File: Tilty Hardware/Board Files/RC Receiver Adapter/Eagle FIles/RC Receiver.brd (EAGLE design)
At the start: 38.1 x 50.8 mm, 19 parts, among them U1 ATMEGA328P, U2 LM2931, Y1 16MHz

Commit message: Finally got TiltyIMU class working! updated some other programs, worked on RC receiver add-on
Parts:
- removed JP5: 18_PIN_HEADER3X6_PTH_HEADER, My Parts:3X6_PTH_HEADER
- added JP7: 18_PIN_HEADER3X6_PTH_HEADER, My Parts:3X6_PTH_HEADER
- added U$1: C74HC407514-SOIC, My Parts:14-SOIC
- Y1: device SparkFun-FreqCtrl:HC49UP -> SparkFun-FreqCtrl:CRYSTAL-SMD-5X3
- moved R3 91.3 mm to (-52.1, 52.1), turned to 0 degrees
- moved R2 86.1 mm to (-48.3, 52.1), turned to 0 degrees
- moved JP6 61.3 mm to (-36.8, 34.3), turned to 0 degrees
- moved R1 59.7 mm to (-41.9, 43.2), turned to 0 degrees
- moved S1 49.5 mm to (-35.6, 43.2), turned to 0 degrees
- moved C2 31.7 mm to (10.0, 37.1), turned to 270 degrees
- moved C6 26.4 mm to (2.54, 7.62)
- moved U2 25.7 mm to (7.62, 6.86), turned to 180 degrees
- moved Y1 21.8 mm to (11.2, 32.5), turned to 90 degrees
- moved C1 19.3 mm to (14.0, 31.2)
- moved C7 18.2 mm to (11.9, 10.4)
- moved C3 7.52 mm to (18.3, 19.3), turned to 0 degrees
- moved U1 5.08 mm to (19.1, 25.4), turned to 270 degrees
- moved SJ1 0.40 mm to (5.97, 13.8)
- turned JP4 to 90 degrees
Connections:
- new net EVEN_CHAN: U$1.P$12, U1.1
- new net ODD_CHAN: U$1.P$4, U1.32
- net +5V: now also JP7.11, JP7.14, JP7.17, JP7.2, JP7.5, JP7.8, U$1.P$14; no longer JP5.11, JP5.14, JP5.17, JP5.2, JP5.5, JP5.8
- net GND: now also JP7.12, JP7.15, JP7.18, JP7.3, JP7.6, JP7.9, U$1.P$13; no longer JP5.12, JP5.15, JP5.18, JP5.3, JP5.6, JP5.9
- net N$1: now also Y1.3; no longer Y1.2
- net SIGNAL_1: now also JP7.1, U$1.P$1; no longer JP5.1, U1.32
- net SIGNAL_2: now also JP7.4, U$1.P$11; no longer JP5.4, U1.1
- net SIGNAL_3: now also JP7.7, U$1.P$2; no longer JP5.7, U1.2
- net SIGNAL_4: now also JP7.10, U$1.P$10; no longer JP5.10, U1.9
- net SIGNAL_5: now also JP7.13, U$1.P$3; no longer JP5.13, U1.10
- net SIGNAL_6: now also JP7.16, U$1.P$9; no longer JP5.16, U1.11
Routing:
- net GND: track 12.7 -> 0.00 mm
- net +5V: track 12.7 -> 0.00 mm

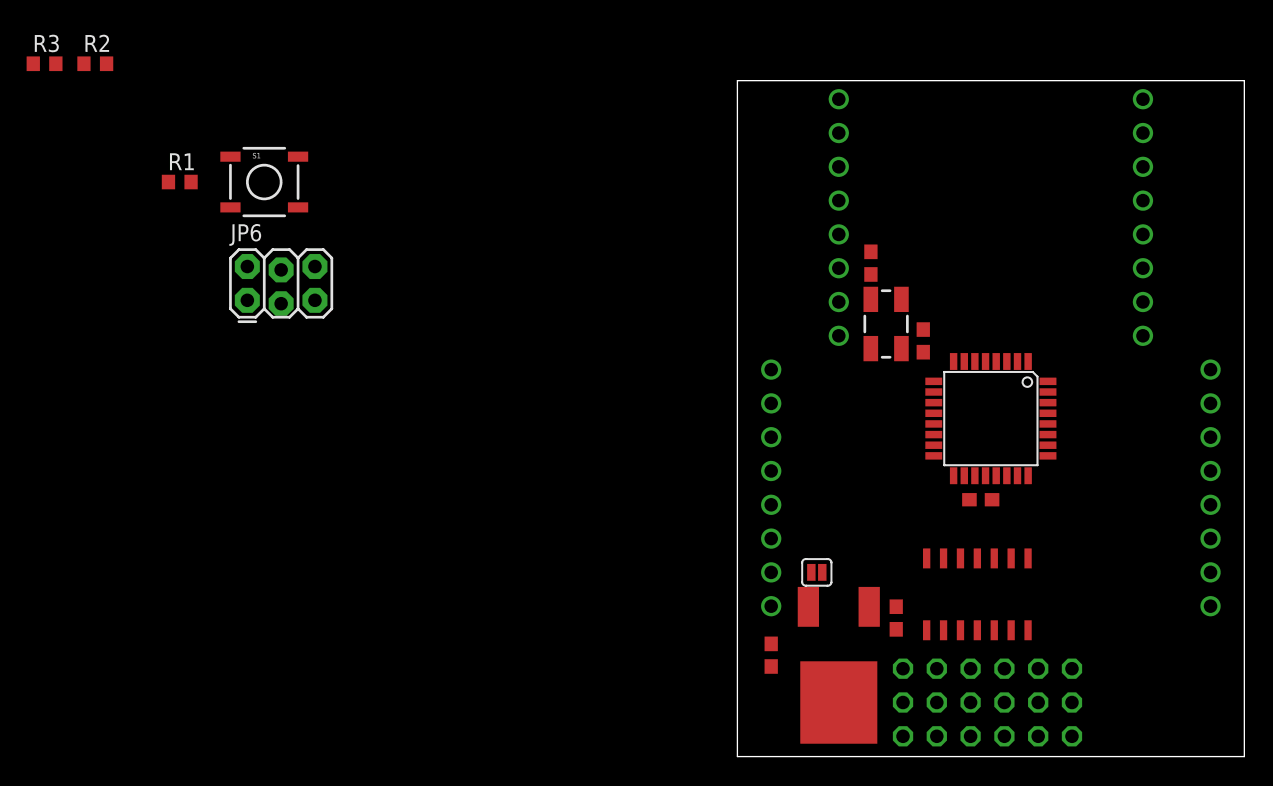
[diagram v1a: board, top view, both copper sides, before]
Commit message: Nearly finished R/C receiver add-on, updated things to-do
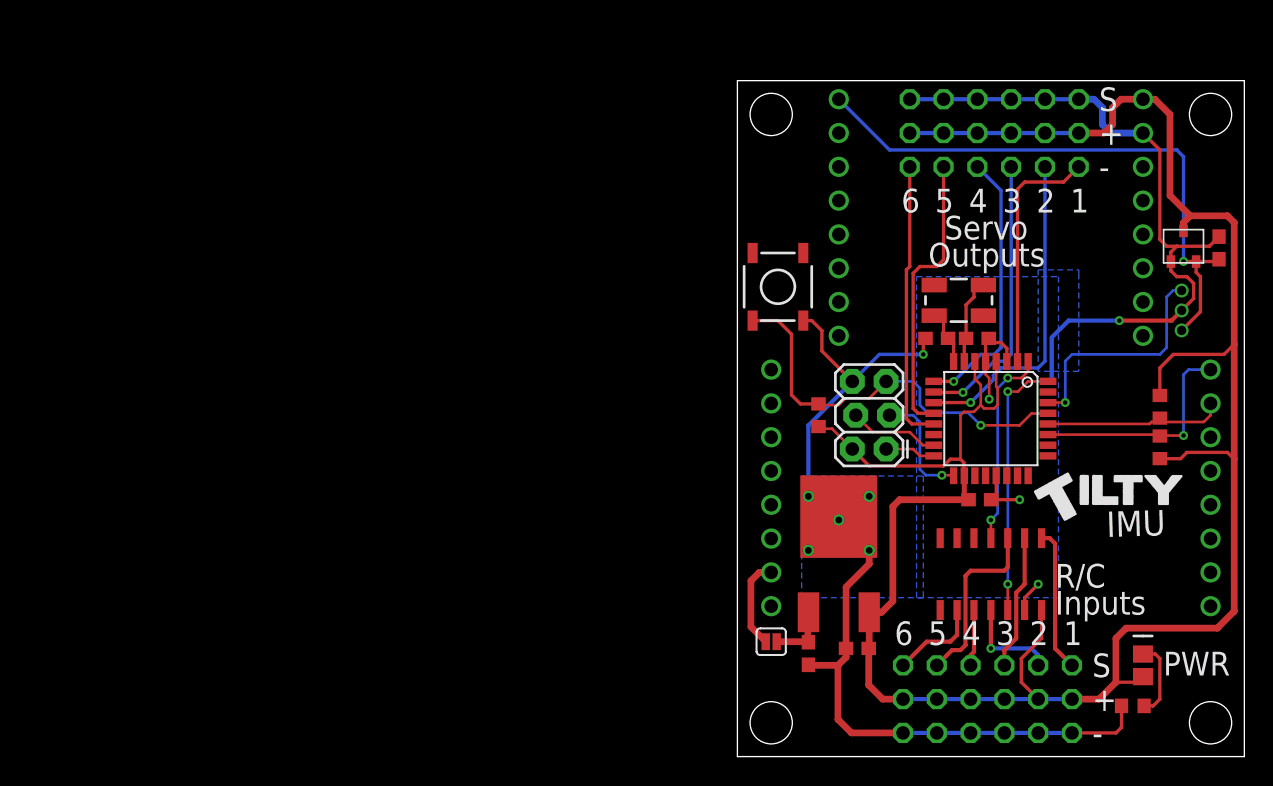
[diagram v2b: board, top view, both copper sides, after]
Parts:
- removed U$1: C74HC407514-SOIC, My Parts:14-SOIC
- added C4: 0.1uF, resistor:C0603
- added D1: (no value), SparkFun-LED:LED-0805
- added JP5: Output, My Parts:3X6_PTH_HEADER
- added JP8: 3-PIN_JST_ZH_PTH_CONNECTORRIGHT_ANGLE_PTH, My Parts:3-PIN_JST_ZH_CONNECTOR_TH
- added R4: 220, resistor:R0603
- added U3: AP7313SOT23R, My Parts:SOT23
- added U4: C74HC407514-SOIC, My Parts:14-SOIC
- JP7: value 18_PIN_HEADER3X6_PTH_HEADER -> Input
- moved R3 87.7 mm to (31.8, 26.3), turned to 90 degrees
- moved R2 85.0 mm to (31.8, 23.2), turned to 270 degrees
- moved R1 51.1 mm to (6.10, 25.7), turned to 90 degrees
- moved JP6 49.3 mm to (11.2, 23.1), turned to 90 degrees
- moved S1 39.4 mm to (3.05, 35.3), turned to 90 degrees
- moved C2 9.80 mm to (18.0, 31.4), turned to 180 degrees
- moved U2 8.38 mm to (7.62, 15.2), turned to 0 degrees
- moved C7 7.12 mm to (5.33, 7.75)
- moved C6 6.50 mm to (9.02, 8.13), turned to 180 degrees
- moved SJ1 6.23 mm to (2.54, 8.64)
- moved Y1 5.74 mm to (16.6, 34.3), turned to 0 degrees
- moved C1 1.03 mm to (15.0, 31.4), turned to 0 degrees
- moved JP7 0.25 mm to (18.8, 4.32)
- moved C3 0.06 mm to (18.2, 19.3)
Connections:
- new net +3V3: C4.1, JP1.8, JP8.P$1, U3.P$2
- new net N$8: D1.2, R4.2
- new net SATELLITE_TX: JP8.P$3, U1.30
- new net SERVO_1: JP5.1, U1.13
- new net SERVO_2: JP5.4, U1.12
- new net SERVO_3: JP5.7, U1.9
- new net SERVO_4: JP5.10, U1.10
- new net SERVO_5: JP5.13, U1.11
- new net SERVO_6: JP5.16, U1.2
- net +5V: now also D1.1, JP4.8, JP5.11, JP5.14, JP5.17, JP5.2, JP5.5, JP5.8, U3.P$3, U4.P$14; no longer U$1.P$14
- net EVEN_CHAN: now also U1.32, U4.P$12; no longer U$1.P$12, U1.1
- net GND: now also C4.2, JP4.7, JP5.12, JP5.15, JP5.18, JP5.3, JP5.6, JP5.9, JP8.P$2, R4.1, U3.P$1, U4.P$13; no longer U$1.P$13
- net ODD_CHAN: now also U1.1, U4.P$4; no longer U$1.P$4, U1.32
- net SIGNAL_1: now also U4.P$1; no longer U$1.P$1
- net SIGNAL_2: now also U4.P$11; no longer U$1.P$11
- net SIGNAL_3: now also U4.P$2; no longer U$1.P$2
- net SIGNAL_4: now also U4.P$10; no longer U$1.P$10
- net SIGNAL_5: now also U4.P$3; no longer U$1.P$3
- net SIGNAL_6: now also U4.P$9; no longer U$1.P$9
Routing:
- net +5V: track 0.00 -> 170.6 mm
- net GND: track 0.00 -> 130.5 mm, vias 0 -> 10
- net +3V3: track 0.00 -> 44.2 mm, vias 0 -> 1
- net RESET: track 0.00 -> 30.8 mm, vias 0 -> 1
- net SERVO_5: track 0.00 -> 24.4 mm, vias 0 -> 1
- net SERVO_2: track 0.00 -> 21.6 mm
- net SERVO_1: track 0.00 -> 21.3 mm
- net SERVO_4: track 0.00 -> 21.1 mm, vias 0 -> 1
- net SERVO_3: track 0.00 -> 20.4 mm, vias 0 -> 1
- net EVEN_CHAN: track 0.00 -> 19.8 mm, vias 0 -> 2
- net SERVO_6: track 0.00 -> 18.2 mm
- net SATELLITE_TX: track 0.00 -> 17.6 mm, vias 0 -> 1
- net SDA: track 0.00 -> 17.0 mm, vias 0 -> 1
- net ODD_CHAN: track 0.00 -> 15.0 mm, vias 0 -> 2
- net SIGNAL_5: track 0.00 -> 13.6 mm
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- added copper zone on layer 16, net GND
- added copper zone on layer 16, net N$3
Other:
- board text added: "+"
- board text added: "-"
- board text added: "1"
- board text added: "2"
- board text added: "3"
- board text added: "4"
- board text added: "5"
- board text added: "6"
- board text added: "Add-on"
- board text added: "IMU"
- board text added: "Inputs"
- board text added: "Outputs"
- board text added: "PWR"
- board text added: "R/C"
- board text added: "R/C Receiver"
- board text added: "S"
- board text added: "Servo"

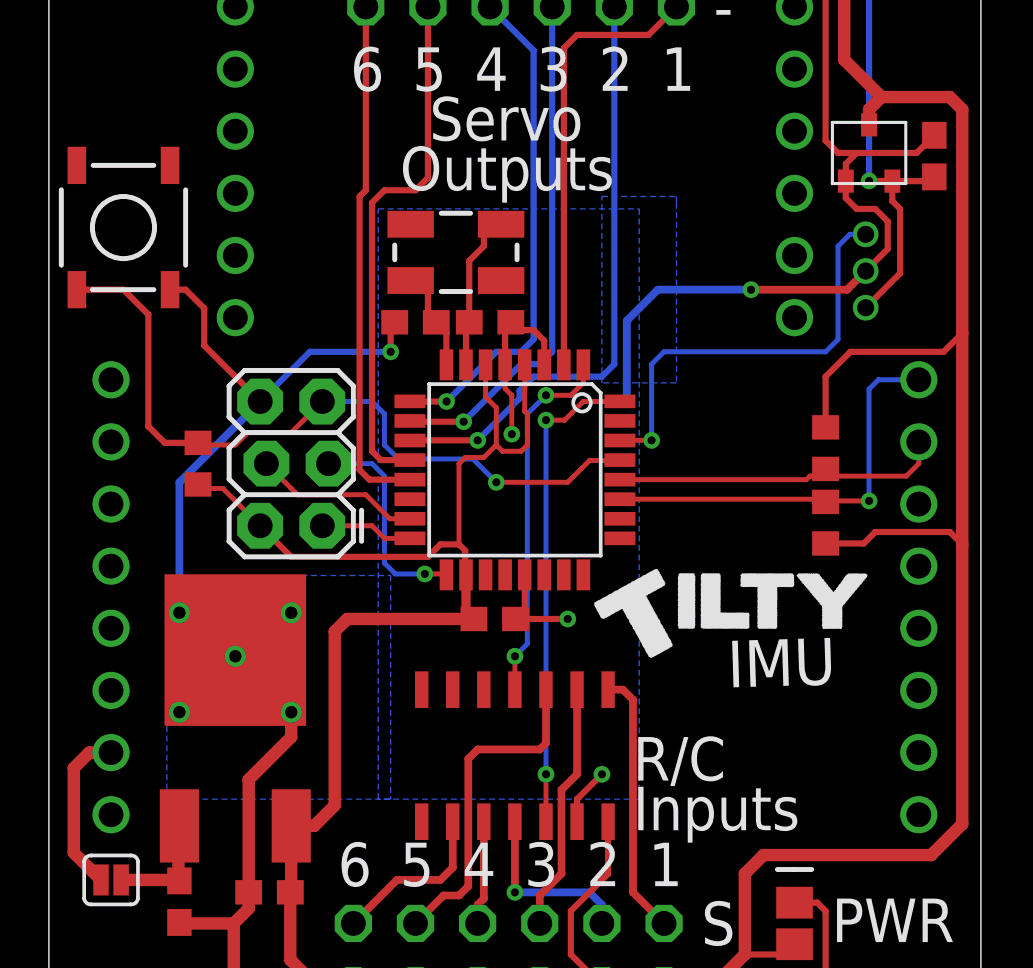
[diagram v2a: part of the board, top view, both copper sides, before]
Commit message: Nearly finished RC Receiver add-on prototype, worked on TiltyIMU library
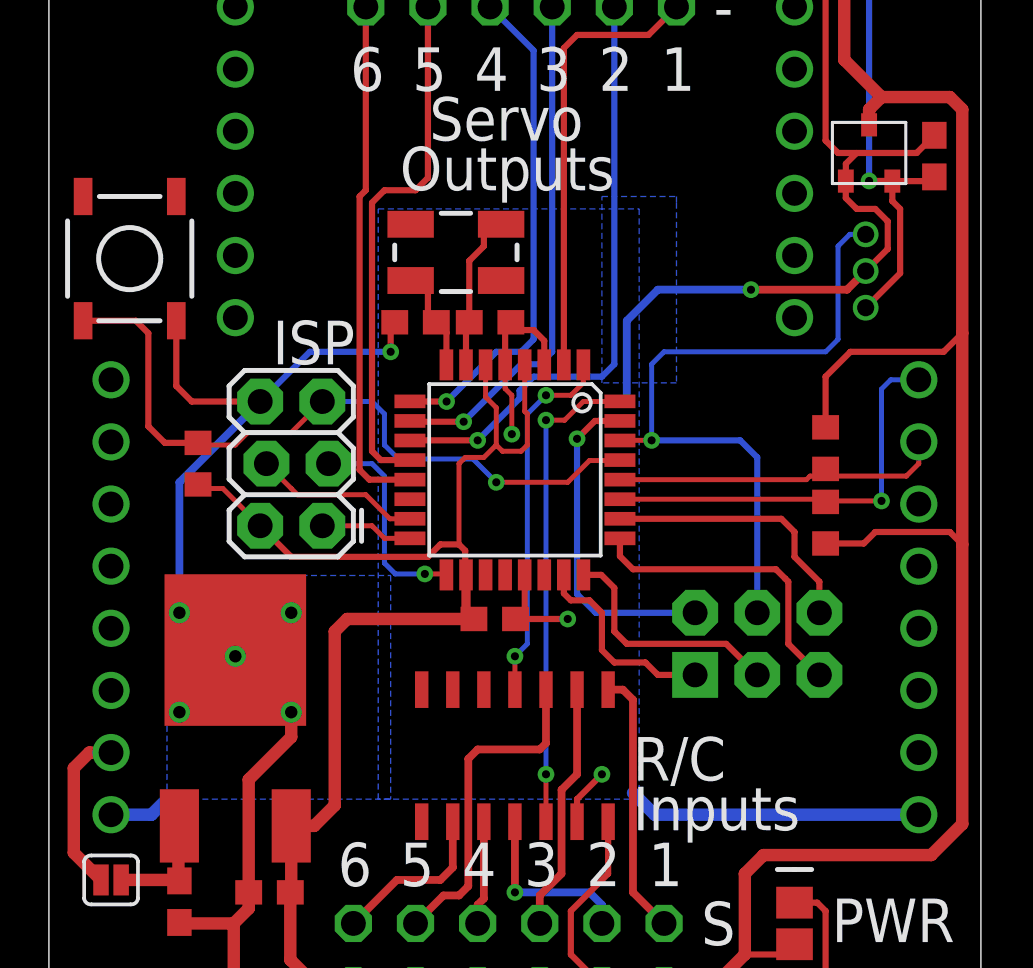
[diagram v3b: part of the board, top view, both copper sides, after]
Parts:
- added JP10: (no value), SparkFun-Connectors:2X3-NS
- moved S1 1.30 mm to (3.30, 34.0)
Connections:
- new net A0: JP10.1, U1.23
- new net A1: JP10.3, U1.24
- new net A2: JP10.5, U1.25
- new net A3: JP10.6, U1.26
- new net ARDUINO_TX: JP10.2, U1.31
- net GND: now also JP2.1, JP3.1
- net SATELLITE_TX: now also JP10.4
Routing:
- net GND: track 130.5 -> 145.0 mm
- net ARDUINO_TX: track 0.00 -> 13.5 mm, vias 0 -> 1
- net A2: track 0.00 -> 12.4 mm
- net A3: track 0.00 -> 11.1 mm
- net SATELLITE_TX: track 17.6 -> 28.5 mm
- net A1: track 0.00 -> 9.84 mm
- net A0: track 0.00 -> 8.40 mm
- net RESET: track 30.8 -> 29.6 mm
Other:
- board text added: "A0"
- board text added: "A1"
- board text added: "A2"
- board text added: "A3"
- board text added: "Extra"
- board text added: "ISP"
- board text added: "Pins"
- board text added: "RX"
- board text added: "TX"

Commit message: Changed a filter cap value, Lots of bluetooth library work
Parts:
- C6: value 0.1uF -> 4.7uF
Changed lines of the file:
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@@
 <element name="JP3" library="pinhead" package="1X08_NO_SS" value="" x="35.56" y="20.193" rot="R90"/>
 <element name="JP4" library="pinhead" package="1X08_NO_SS" value="" x="30.48" y="40.513" rot="R90"/>
-<element name="C6" library="resistor" package="C0603" value="0.1uF" x="9.017" y="8.128" smashed="yes" rot="R180"/>
+<element name="C6" library="resistor" package="C0603" value="4.7uF" x="9.017" y="8.128" smashed="yes" rot="R180"/>
 <element name="C7" library="resistor" package="C0603" value="0.1uF" x="5.334" y="7.747" smashed="yes" rot="R270"/>
 <element name="SJ1" library="SparkFun-Passives" package="SJ_2S" value="SOLDERJUMPERNC" x="2.54" y="8.636" smashed="yes"/>
